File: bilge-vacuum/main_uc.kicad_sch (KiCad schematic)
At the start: 15 parts, among them J1 TC2030-SWD, SW1 SW_Push, U1 STM32G0B1CEU6

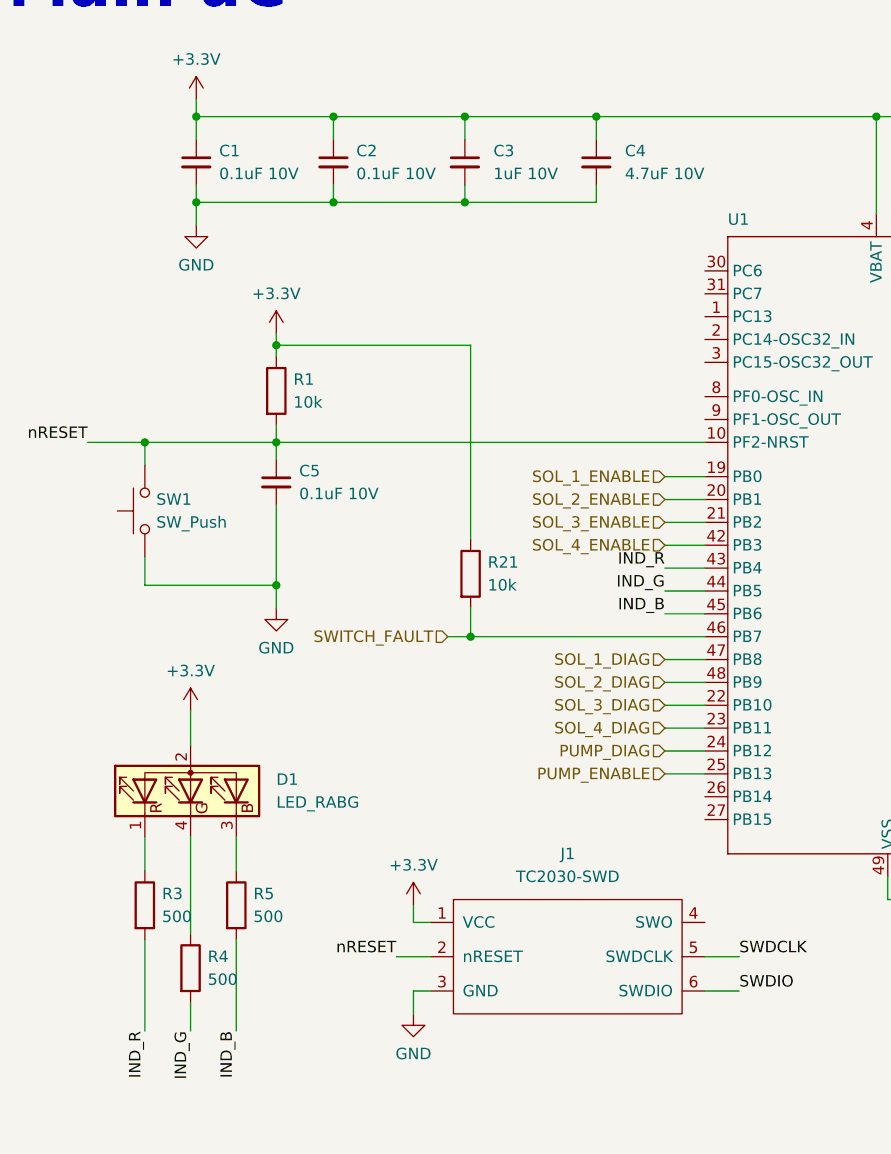
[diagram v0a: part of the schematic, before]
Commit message: Assign the bulk of parts, some passives still need custom footprints.
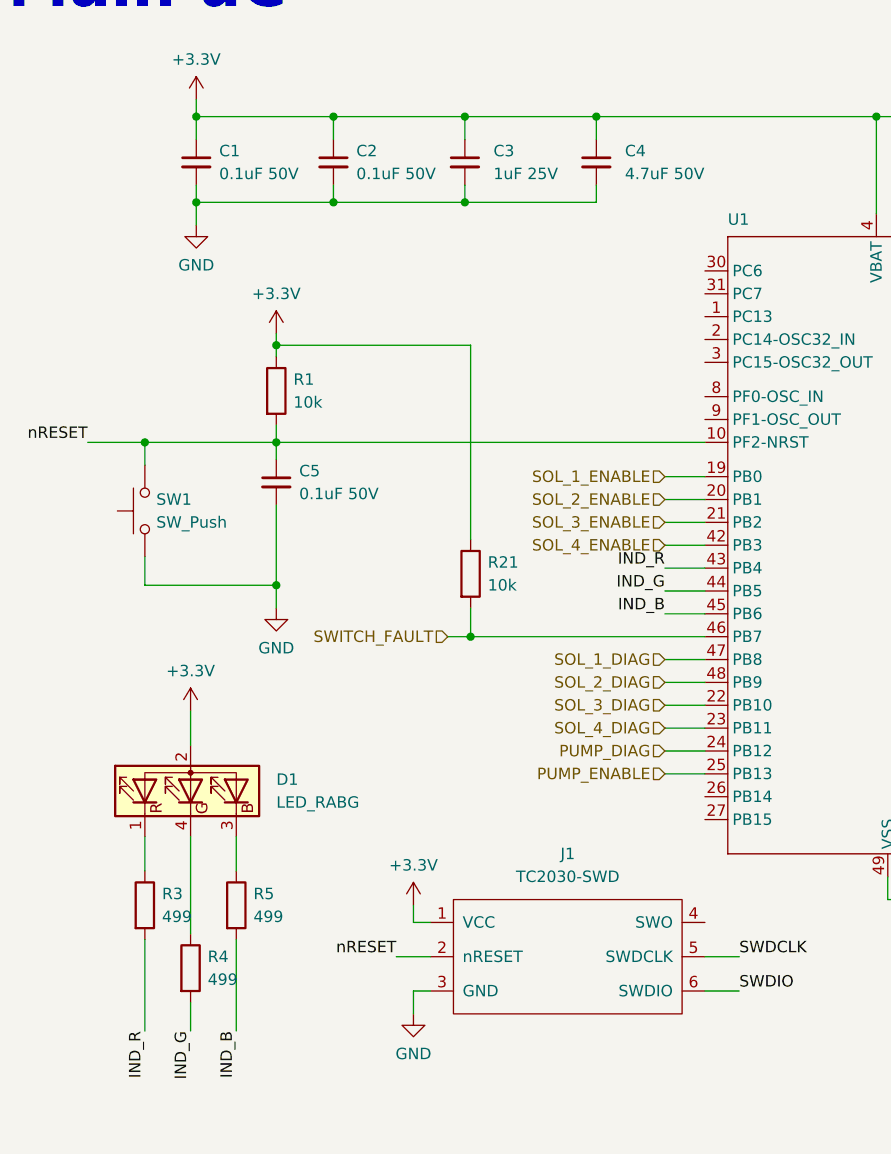
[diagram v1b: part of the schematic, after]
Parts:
- C1, C2, C5: value 0.1uF 10V -> 0.1uF 50V; footprint (none) -> Capacitor_SMD:C_0805_2012Metric
- C3: value 1uF 10V -> 1uF 25V; footprint (none) -> Capacitor_SMD:C_0805_2012Metric
- C4: value 4.7uF 10V -> 4.7uF 50V; footprint (none) -> Capacitor_SMD:C_0805_2012Metric
- D1: footprint (none) -> LED_SMD:LED_Cree-PLCC4_3.2x2.8mm_CCW
- R1, R21: footprint (none) -> Resistor_SMD:R_0805_2012Metric
- R3, R4, R5: value 500 -> 499; footprint (none) -> Resistor_SMD:R_0805_2012Metric
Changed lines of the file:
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@@
       (effects (font (size 1.27 1.27)) (justify left))
     )
-    (property "Footprint" "" (at 75.057 93.98 90)
+    (property "Footprint" "Resistor_SMD:R_0805_2012Metric" (at 75.057 93.98 90)
       (effects (font (size 1.27 1.27)) hide)
     )
@@
       (effects (font (size 1.27 1.27)) (justify left))
     )
-    (property "Value" "0.1uF 10V" (at 57.785 85.0963 0)
-      (effects (font (size 1.27 1.27)) (justify left))
-    )
-    (property "Footprint" "" (at 55.245 83.82 0)
+    (property "Value" "0.1uF 50V" (at 57.785 85.0963 0)
+      (effects (font (size 1.27 1.27)) (justify left))
+    )
+    (property "Footprint" "Capacitor_SMD:C_0805_2012Metric" (at 55.245 83.82 0)
       (effects (font (size 1.27 1.27)) hide)
     )
@@
       (effects (font (size 1.27 1.27)) (justify left))
     )
-    (property "Value" "1uF 10V" (at 79.375 49.5363 0)
-      (effects (font (size 1.27 1.27)) (justify left))
-    )
-    (property "Footprint" "" (at 76.2 48.26 0)
+    (property "Value" "1uF 25V" (at 79.375 49.5363 0)
+      (effects (font (size 1.27 1.27)) (justify left))
+    )
+    (property "Footprint" "Capacitor_SMD:C_0805_2012Metric" (at 76.2 48.26 0)
       (effects (font (size 1.27 1.27)) hide)
     )
@@
       (effects (font (size 1.27 1.27)) (justify left))
     )
-    (property "Value" "0.1uF 10V" (at 64.135 49.5363 0)
-      (effects (font (size 1.27 1.27)) (justify left))
-    )
-    (property "Footprint" "" (at 61.595 48.26 0)
+    (property "Value" "0.1uF 50V" (at 64.135 49.5363 0)
+      (effects (font (size 1.27 1.27)) (justify left))
+    )
+    (property "Footprint" "Capacitor_SMD:C_0805_2012Metric" (at 61.595 48.26 0)
       (effects (font (size 1.27 1.27)) hide)
     )
@@
       (effects (font (size 1.27 1.27)) (justify left))
     )
-    (property "Value" "500" (at 42.545 132.08 0)
-      (effects (font (size 1.27 1.27)) (justify left))
-    )
-    (property "Footprint" "" (at 38.862 130.81 90)
+    (property "Value" "499" (at 42.545 132.08 0)
+      (effects (font (size 1.27 1.27)) (justify left))
+    )
+    (property "Footprint" "Resistor_SMD:R_0805_2012Metric" (at 38.862 130.81 90)
       (effects (font (size 1.27 1.27)) hide)
     )
@@
       (effects (font (size 1.27 1.27)) (justify left))
     )
-    (property "Value" "500" (at 47.625 139.065 0)
-      (effects (font (size 1.27 1.27)) (justify left))
-    )
-    (property "Footprint" "" (at 43.942 137.795 90)
+    (property "Value" "499" (at 47.625 139.065 0)
+      (effects (font (size 1.27 1.27)) (justify left))
+    )
+    (property "Footprint" "Resistor_SMD:R_0805_2012Metric" (at 43.942 137.795 90)
       (effects (font (size 1.27 1.27)) hide)
     )
@@
       (effects (font (size 1.27 1.27)) (justify left))
     )
-    (property "Value" "4.7uF 10V" (at 93.98 49.5363 0)
-      (effects (font (size 1.27 1.27)) (justify left))
-    )
-    (property "Footprint" "" (at 90.805 48.26 0)
+    (property "Value" "4.7uF 50V" (at 93.98 49.5363 0)
+      (effects (font (size 1.27 1.27)) (justify left))
+    )
+    (property "Footprint" "Capacitor_SMD:C_0805_2012Metric" (at 90.805 48.26 0)
       (effects (font (size 1.27 1.27)) hide)
     )
@@
       (effects (font (size 1.27 1.27)) (justify left))
     )
-    (property "Value" "0.1uF 10V" (at 48.895 49.5363 0)
-      (effects (font (size 1.27 1.27)) (justify left))
-    )
-    (property "Footprint" "" (at 46.355 48.26 0)
+    (property "Value" "0.1uF 50V" (at 48.895 49.5363 0)
+      (effects (font (size 1.27 1.27)) (justify left))
+    )
+    (property "Footprint" "Capacitor_SMD:C_0805_2012Metric" (at 46.355 48.26 0)
       (effects (font (size 1.27 1.27)) hide)
     )
@@
       (effects (font (size 1.27 1.27)) (justify left))
     )
-    (property "Footprint" "" (at 53.467 73.66 90)
+    (property "Footprint" "Resistor_SMD:R_0805_2012Metric" (at 53.467 73.66 90)
       (effects (font (size 1.27 1.27)) hide)
     )
@@
       (effects (font (size 1.27 1.27)) (justify left))
     )
-    (property "Value" "500" (at 52.705 132.08 0)
-      (effects (font (size 1.27 1.27)) (justify left))
-    )
-    (property "Footprint" "" (at 49.022 130.81 90)
+    (property "Value" "499" (at 52.705 132.08 0)
+      (effects (font (size 1.27 1.27)) (justify left))
+    )
+    (property "Footprint" "Resistor_SMD:R_0805_2012Metric" (at 49.022 130.81 90)
       (effects (font (size 1.27 1.27)) hide)
     )
@@
       (effects (font (size 1.27 1.27)) (justify right))
     )
-    (property "Footprint" "" (at 46.99 118.11 0)
-      (effects (font (size 1.27 1.27)) hide)
-    )
+    (property "Footprint" "LED_SMD:LED_Cree-PLCC4_3.2x2.8mm_CCW" (at 46.99 118.11 0)
+      (effects (font (size 1.27 1.27)) hide)
+    )

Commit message: Vac progress
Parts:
- added BZ1: PKLCS1212E40A1-R1, Custom Parts:PKLCS1212E40A1-R1, symbol Device:Buzzer
- added Q8: Q_NMOS_GSD, Package_TO_SOT_SMD:SOT-23-3, symbol Device:Q_NMOS_GSD
- added R1 (x5): 10k, Resistor_SMD:R_0805_2012Metric, symbol Device:R
- added R1 (x2): 10, Resistor_SMD:R_0805_2012Metric, symbol Device:R
- added R1: 1k, Resistor_SMD:R_0805_2012Metric, symbol Device:R
- added S1: JS5208, Custom Parts:JS5208, symbol Custom Parts:JS5208
- J1: footprint Custom:TC2030-IDC-FP -> Custom Parts:TC2030-IDC-FP
- R2: now not fitted
- SW1: value SW_Push -> B3F-1000; footprint (none) -> Button_Switch_THT:SW_PUSH_6mm
- U1: footprint Custom:UFQFPN-48 -> Custom Parts:UFQFPN-48
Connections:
- net +3.3V: now also R1.1, R1.1, R1.1, R1.1, R1.1, R1.1
- net GND: now also Q8.2 (S), S1. (COM)
- net NAV_A: now reaches U1.12 (PA1)
- net NAV_A: now also R1.2, S1.4 (A)
- net NAV_B: now reaches U1.13 (PA2)
- net NAV_B: now also R1.2, S1.2 (B)
- net NAV_SEL: now reaches U1.14 (PA3)
- net NAV_SEL: now also R1.2, S1.3 (SEL)
- net NAV_D: now reaches U1.15 (PA4)
- net NAV_D: now also R1.2, S1.5 (D)
- net BUZZER_DRIVE: now reaches U1.30 (PC6)
- net BUZZER_DRIVE: now also R1.1
- net NAV_C: now reaches U1.37 (PA15)
- net NAV_C: now also R1.2, S1.6 (C)
- new net: BZ1.1 (-), R1.2, R1.2
- new net: BZ1.2 (+), Q8.3 (D), R1.1
- new net: Q8.1 (G), R1.2

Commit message: bilge vac 1v0
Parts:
- R2: footprint (none) -> Resistor_SMD:R_0805_2012Metric
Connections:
- net GND: now also S1.1 (COM); no longer S1. (COM)
- net +3.3V renamed +3V3
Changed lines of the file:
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@@
     )
   )
-  (symbol (lib_id "power:+3.3V") (at 46.355 41.275 0) (unit 1)
+  (symbol (lib_id "power:+3V3") (at 46.355 41.275 0) (unit 1)
     (in_bom yes) (on_board yes) (dnp no) (fields_autoplaced)
     (property "Reference" "#PWR02" (at 46.355 45.085 0)
       (effects (font (size 1.27 1.27)) hide)
     )
-    (property "Value" "+3.3V" (at 46.355 36.83 0)
+    (property "Value" "+3V3" (at 46.355 37.719 0)
       (effects (font (size 1.27 1.27)))
     )
@@
     )
   )
-  (symbol (lib_id "power:+3.3V") (at 45.72 109.22 0) (unit 1)
+  (symbol (lib_id "power:+3V3") (at 45.72 109.22 0) (unit 1)
     (in_bom yes) (on_board yes) (dnp no) (fields_autoplaced)
     (property "Reference" "#PWR07" (at 45.72 113.03 0)
       (effects (font (size 1.27 1.27)) hide)
     )
-    (property "Value" "+3.3V" (at 45.72 104.775 0)
+    (property "Value" "+3V3" (at 45.72 105.664 0)
       (effects (font (size 1.27 1.27)))
     )
@@
     )
   )
-  (symbol (lib_id "power:+3.3V") (at 55.245 67.31 0) (unit 1)
+  (symbol (lib_id "power:+3V3") (at 55.245 67.31 0) (unit 1)
     (in_bom yes) (on_board yes) (dnp no) (fields_autoplaced)
     (property "Reference" "#PWR04" (at 55.245 71.12 0)
       (effects (font (size 1.27 1.27)) hide)
     )
-    (property "Value" "+3.3V" (at 55.245 62.865 0)
+    (property "Value" "+3V3" (at 55.245 63.754 0)
       (effects (font (size 1.27 1.27)))
     )
@@
     )
   )
-  (symbol (lib_id "power:+3.3V") (at 70.485 130.81 0) (unit 1)
+  (symbol (lib_id "power:+3V3") (at 70.485 130.81 0) (unit 1)
     (in_bom yes) (on_board yes) (dnp no) (fields_autoplaced)
     (property "Reference" "#PWR09" (at 70.485 134.62 0)
       (effects (font (size 1.27 1.27)) hide)
     )
-    (property "Value" "+3.3V" (at 70.485 126.365 0)
+    (property "Value" "+3V3" (at 70.485 127.254 0)
       (effects (font (size 1.27 1.27)))
     )
@@
       (effects (font (size 1.27 1.27)) (justify left))
     )
-    (property "Footprint" "" (at 167.132 109.855 90)
+    (property "Footprint" "Resistor_SMD:R_0805_2012Metric" (at 167.132 109.855 90)
       (effects (font (size 1.27 1.27)) hide)
     )
@@
       (effects (font (size 1.27 1.27)) hide)
     )
-    (pin "")
+    (pin "1")
     (pin "2")
     (pin "3")
@@
     )
   )
-  (symbol (lib_id "power:+3.3V") (at 193.675 116.205 0) (unit 1)
+  (symbol (lib_id "power:+3V3") (at 193.675 116.205 0) (unit 1)
     (in_bom yes) (on_board yes) (dnp no) (fields_autoplaced)
     (property "Reference" "#PWR02" (at 193.675 120.015 0)
       (effects (font (size 1.27 1.27)) hide)
     )
-    (property "Value" "+3.3V" (at 193.675 111.76 0)
-      (effects (font (size 1.27 1.27)))
-    )
+    (property "Value" "+3V3" (at 193.675 112.649 0)
+      (effects (font (size 1.27 1.27)))
+    )

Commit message: Fixes
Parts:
- R1, R21: value 10k -> 10k 1%
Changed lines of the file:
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@@
       (effects (font (size 1.27 1.27)) (justify left))
     )
-    (property "Value" "10k" (at 78.74 95.25 0)
+    (property "Value" "10k 1%" (at 78.74 95.25 0)
       (effects (font (size 1.27 1.27)) (justify left))
     )
@@
       (effects (font (size 1.27 1.27)) (justify left))
     )
-    (property "Value" "10k" (at 238.76 57.785 0)
+    (property "Value" "10k 1%" (at 238.76 57.785 0)
       (effects (font (size 1.27 1.27)) (justify left))
     )
@@
       (effects (font (size 1.27 1.27)) (justify left))
     )
-    (property "Value" "10k" (at 223.52 57.785 0)
+    (property "Value" "10k 1%" (at 223.52 57.785 0)
       (effects (font (size 1.27 1.27)) (justify left))
     )
@@
       (effects (font (size 1.27 1.27)) (justify left))
     )
-    (property "Value" "10k" (at 231.14 57.785 0)
+    (property "Value" "10k 1%" (at 231.14 57.785 0)
       (effects (font (size 1.27 1.27)) (justify left))
     )
@@
       (effects (font (size 1.27 1.27)) (justify left))
     )
-    (property "Value" "10k" (at 183.515 58.42 0)
+    (property "Value" "10k 1%" (at 183.515 58.42 0)
       (effects (font (size 1.27 1.27)) (justify left))
     )
@@
       (effects (font (size 1.27 1.27)) (justify left))
     )
-    (property "Value" "10k" (at 57.15 74.93 0)
+    (property "Value" "10k 1%" (at 57.15 74.93 0)
       (effects (font (size 1.27 1.27)) (justify left))
     )
@@
       (effects (font (size 1.27 1.27)) (justify left))
     )
-    (property "Value" "10k" (at 191.77 58.42 0)
-      (effects (font (size 1.27 1.27)) (justify left))
-    )
+    (property "Value" "10k 1%" (at 191.77 58.42 0)
+      (effects (font (size 1.27 1.27)) (justify left))
+    )

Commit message: Fixes
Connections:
- net DISPLAY_3V0_ENABLE: now reaches U1.31 (PC7)
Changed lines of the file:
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@@
+    (stroke (width 0) (type default))
+  )
+  (wire (pts (xy 99.06 62.865) (xy 102.87 62.865))
     (stroke (width 0) (type default))
   )
@@
     (stroke (width 0) (type default))
   )
-  (rectangle (start 19.05 19.05) (end 247.65 158.75)
+  (rectangle (start 19.05 19.05) (end 254 158.75)
     (stroke (width 0) (type default))
     (fill (type none))
@@
     (effects (font (size 1.27 1.27)) (justify right))
   )
+  (hierarchical_label "DISPLAY_3V0_ENABLE" (shape input) (at 99.06 62.865 180) (fields_autoplaced)
+    (effects (font (size 1.27 1.27)) (justify right))
+  )
